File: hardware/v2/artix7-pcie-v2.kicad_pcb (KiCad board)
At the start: 4 copper layers, 60 x 51 mm, 187 parts, among them J1 Conn_02x20_Odd_Even, J10 USB_B_Micro, J2 Conn_02x20_Odd_Even, J4 USB3_A, J5 USB3_A_AS_PCIE, J6 JTAG, J7 Conn_01x02, J8 SER, SW1 PROG, SW2 USER, U1 XC7A75T-FGG484, U10 TPS74701DRCR, U2 MX25L51245GZ2I-10G, U3 TLV62569DBVR, U4 5P49V6965A000NLGI, U5 TLV62569PDDCR, U6 TLV62569DBVR, U7 TLV62569DBVR, U8 TLV62569DBVR, U9 TPS74701DRCR, X1 25MHz/10pF

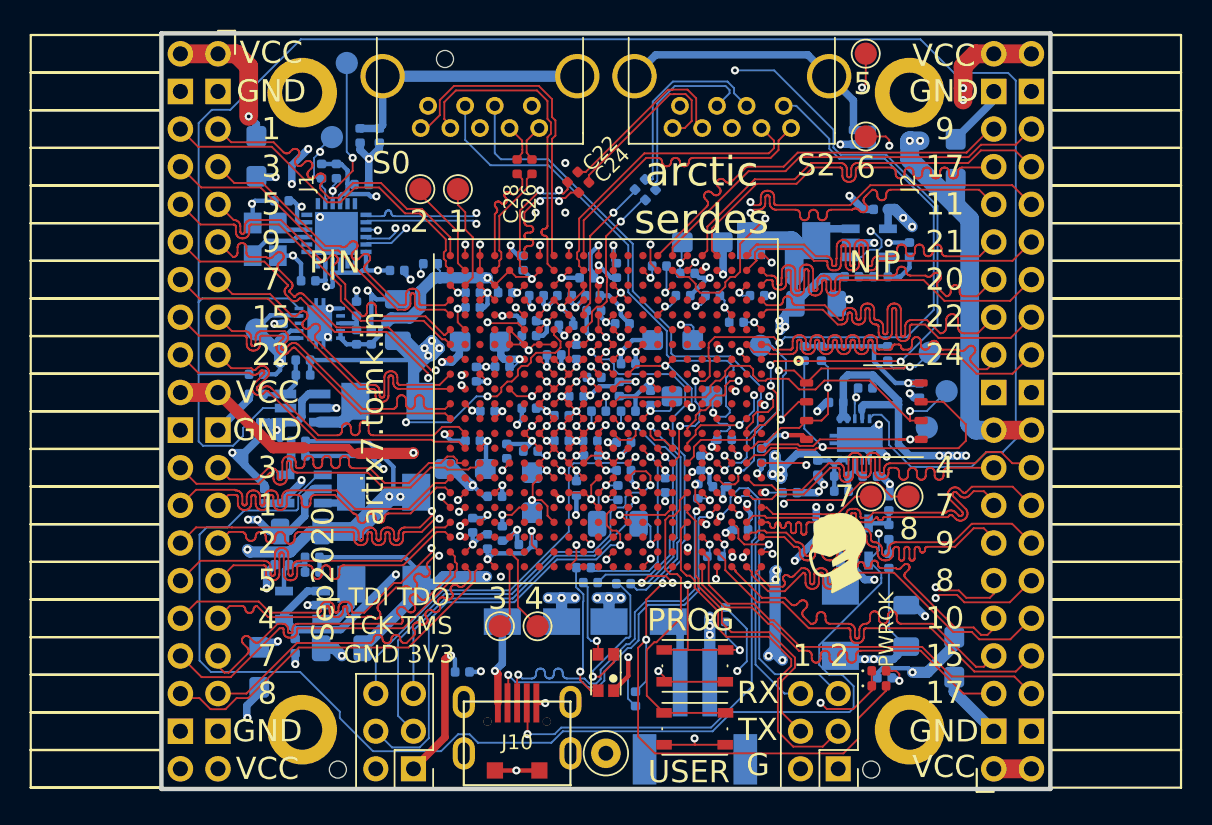
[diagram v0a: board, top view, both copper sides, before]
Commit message: v2 hardware: fixed drc issues from inductor pad changes
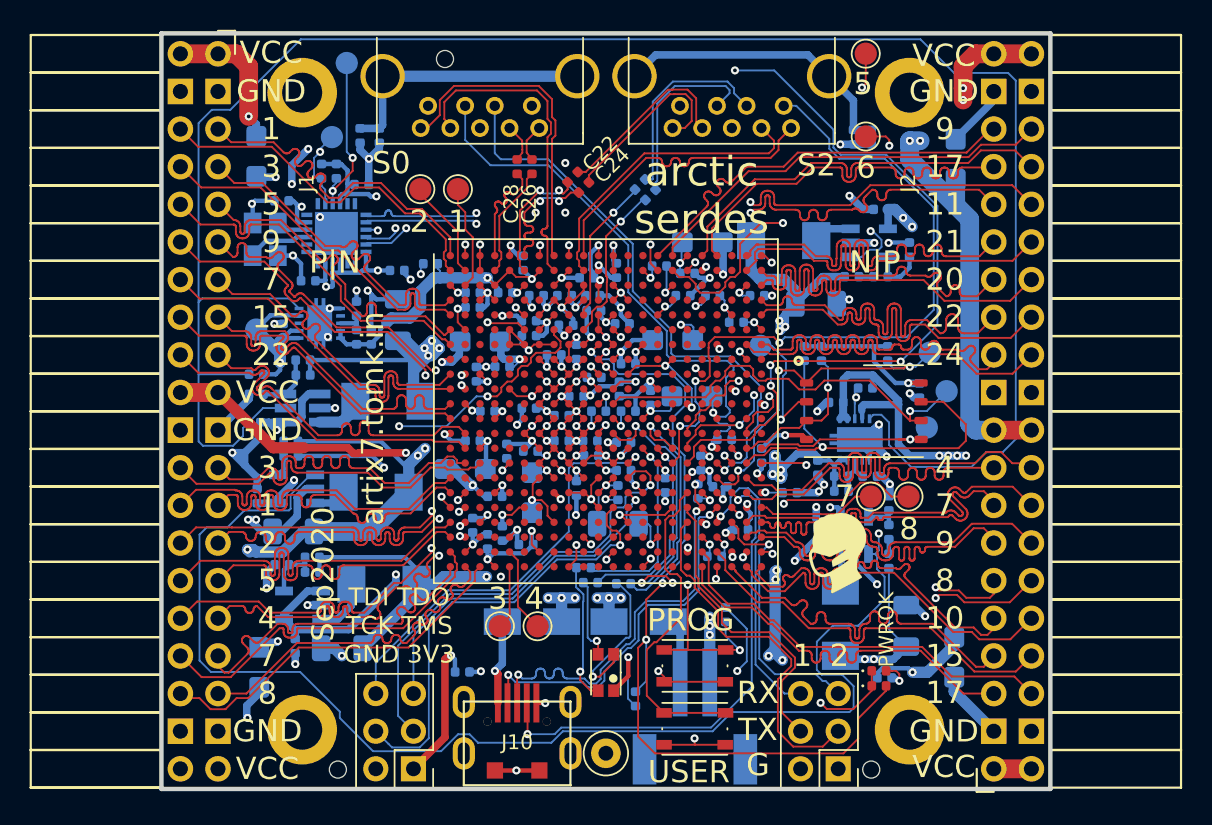
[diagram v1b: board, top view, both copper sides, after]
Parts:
- moved L3 0.51 mm to (125.6, 92.3)
- moved C12 0.51 mm to (120.0, 94.9)
- moved C8 0.51 mm to (117.6, 92.5)
- moved R18 0.51 mm to (119.8, 89.8)
- moved R19 0.51 mm to (119.8, 88.8)
- moved U6 0.51 mm to (120.2, 92.1)
- moved U3 0.45 mm to (157.9, 95.2)
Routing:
- net VCC: track 171.4 -> 169.6 mm
- net /Power/PG_1.8V: track 119.7 -> 121.1 mm
- net GND: track 277.9 -> 278.8 mm
- net /VCCO_16: track 103.0 -> 102.4 mm

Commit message: v2 hardware: change 100uF to 3528 for jlcpcb
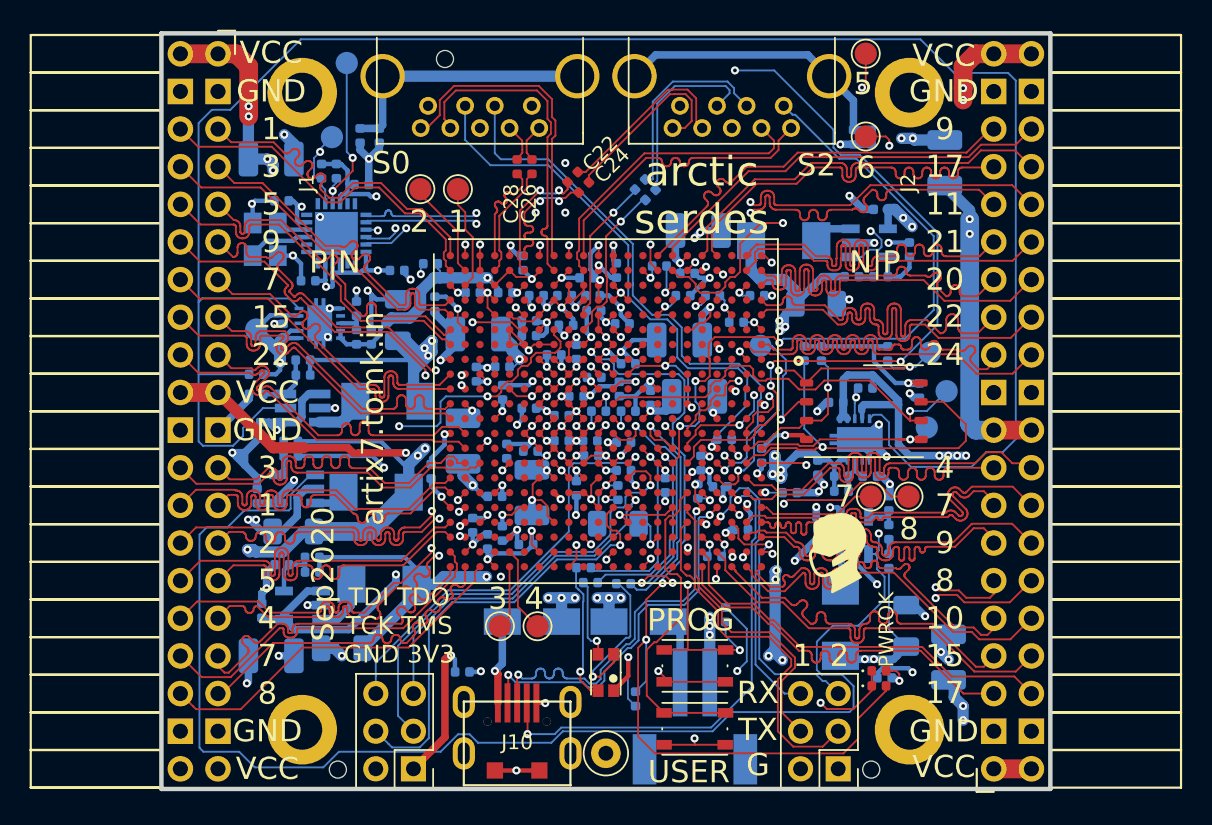
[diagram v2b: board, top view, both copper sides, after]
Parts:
- C18, C23, C42, C44, C60, C67, C68, C78, C85, C86: footprint tom-passives:CP_EIA-3216-12_Kemet-S -> tom-passives:CP_EIA-3528-15_AVX-H
- R26, R27, R34, R35: value 270R/5% -> 300R/5%
- R30: value 1k/1% -> 1.2k/1%
- moved C94 3.48 mm to (129.3, 90.9), turned to 270 degrees
- moved C11 3.29 mm to (117.9, 100.3), turned to 270 degrees
- moved C90 2.56 mm to (129.5, 79.6), turned to 270 degrees
- moved C85 1.89 mm to (131.5, 88.8), turned to 90 degrees
- moved C88 1.63 mm to (134.1, 85.5), turned to 90 degrees
- moved C18 1.12 mm to (118.5, 103.3), turned to 0 degrees
- moved C23 1.01 mm to (118.5, 69.8), turned to 0 degrees
- moved C78 0.84 mm to (147.3, 74.6)
- moved C68 0.77 mm to (164.0, 70.0)
- moved C86 0.52 mm to (132.5, 81.6)
- moved C42 0.46 mm to (146.1, 82.0)
- moved C67 0.38 mm to (164.2, 103.4), turned to 90 degrees
- moved C60 0.17 mm to (147.1, 85.8)
- turned C45 to 180 degrees
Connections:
- U1 pad A13: Net-(U1-PadA13) -> (no net)
- U1 pad A14: Net-(U1-PadA14) -> (no net)
- U1 pad A20: Net-(U1-PadA20) -> (no net)
- U1 pad AA10: Net-(U1-PadAA10) -> (no net)
- U1 pad AA11: Net-(U1-PadAA11) -> (no net)
- U1 pad AA13: Net-(U1-PadAA13) -> (no net)
- U1 pad AA14: Net-(U1-PadAA14) -> (no net)
- U1 pad AA15: Net-(U1-PadAA15) -> (no net)
- U1 pad AA16: Net-(U1-PadAA16) -> (no net)
- U1 pad AA3: Net-(U1-PadAA3) -> (no net)
- U1 pad AA4: Net-(U1-PadAA4) -> (no net)
- U1 pad AA6: Net-(U1-PadAA6) -> (no net)
- U1 pad AA8: Net-(U1-PadAA8) -> (no net)
- U1 pad AA9: Net-(U1-PadAA9) -> (no net)
- U1 pad AB10: Net-(U1-PadAB10) -> (no net)
- U1 pad AB11: Net-(U1-PadAB11) -> (no net)
- U1 pad AB12: Net-(U1-PadAB12) -> (no net)
- U1 pad AB13: Net-(U1-PadAB13) -> (no net)
- U1 pad AB15: Net-(U1-PadAB15) -> (no net)
- U1 pad AB16: Net-(U1-PadAB16) -> (no net)
- U1 pad AB17: Net-(U1-PadAB17) -> (no net)
- U1 pad AB6: Net-(U1-PadAB6) -> (no net)
- U1 pad AB7: Net-(U1-PadAB7) -> (no net)
- U1 pad AB8: Net-(U1-PadAB8) -> (no net)
- U1 pad B13: Net-(U1-PadB13) -> (no net)
- U1 pad B20: Net-(U1-PadB20) -> (no net)
- U1 pad C13: Net-(U1-PadC13) -> (no net)
- U1 pad C14: Net-(U1-PadC14) -> (no net)
- U1 pad C15: Net-(U1-PadC15) -> (no net)
- U1 pad C17: Net-(U1-PadC17) -> (no net)
- U1 pad C18: Net-(U1-PadC18) -> (no net)
- U1 pad C19: Net-(U1-PadC19) -> (no net)
- U1 pad C20: Net-(U1-PadC20) -> (no net)
- U1 pad C5: Net-(U1-PadC5) -> (no net)
- U1 pad C7: Net-(U1-PadC7) -> (no net)
- U1 pad D14: Net-(U1-PadD14) -> (no net)
- U1 pad D15: Net-(U1-PadD15) -> (no net)
- U1 pad D16: Net-(U1-PadD16) -> (no net)
- U1 pad D17: Net-(U1-PadD17) -> (no net)
- U1 pad D19: Net-(U1-PadD19) -> (no net)
- U1 pad D2: Net-(U1-PadD2) -> (no net)
- U1 pad D20: Net-(U1-PadD20) -> (no net)
- U1 pad D21: Net-(U1-PadD21) -> (no net)
- U1 pad D5: Net-(U1-PadD5) -> (no net)
- U1 pad D7: Net-(U1-PadD7) -> (no net)
- U1 pad E13: Net-(U1-PadE13) -> (no net)
- U1 pad E14: Net-(U1-PadE14) -> (no net)
- U1 pad E16: Net-(U1-PadE16) -> (no net)
- U1 pad E17: Net-(U1-PadE17) -> (no net)
- U1 pad E18: Net-(U1-PadE18) -> (no net)
- U1 pad E19: Net-(U1-PadE19) -> (no net)
- U1 pad E2: Net-(U1-PadE2) -> (no net)
- U1 pad E21: Net-(U1-PadE21) -> (no net)
- U1 pad E3: Net-(U1-PadE3) -> (no net)
- U1 pad F13: Net-(U1-PadF13) -> (no net)
- U1 pad F14: Net-(U1-PadF14) -> (no net)
- U1 pad F15: Net-(U1-PadF15) -> (no net)
- U1 pad F16: Net-(U1-PadF16) -> (no net)
- U1 pad F18: Net-(U1-PadF18) -> (no net)
- U1 pad F19: Net-(U1-PadF19) -> (no net)
- U1 pad F20: Net-(U1-PadF20) -> (no net)
- U1 pad F21: Net-(U1-PadF21) -> (no net)
- U1 pad F3: Net-(U1-PadF3) -> (no net)
- U1 pad F4: Net-(U1-PadF4) -> (no net)
- U1 pad G13: Net-(U1-PadG13) -> (no net)
- U1 pad G15: Net-(U1-PadG15) -> (no net)
- U1 pad G16: Net-(U1-PadG16) -> (no net)
- U1 pad G17: Net-(U1-PadG17) -> (no net)
- U1 pad G18: Net-(U1-PadG18) -> (no net)
- U1 pad G2: Net-(U1-PadG2) -> (no net)
- U1 pad G20: Net-(U1-PadG20) -> (no net)
- U1 pad G3: Net-(U1-PadG3) -> (no net)
- U1 pad G4: Net-(U1-PadG4) -> (no net)
- U1 pad H13: Net-(U1-PadH13) -> (no net)
- U1 pad H14: Net-(U1-PadH14) -> (no net)
- U1 pad H15: Net-(U1-PadH15) -> (no net)
- U1 pad H17: Net-(U1-PadH17) -> (no net)
- U1 pad H18: Net-(U1-PadH18) -> (no net)
- U1 pad H19: Net-(U1-PadH19) -> (no net)
- U1 pad H2: Net-(U1-PadH2) -> (no net)
- U1 pad H20: Net-(U1-PadH20) -> (no net)
- U1 pad H22: Net-(U1-PadH22) -> (no net)
- U1 pad H3: Net-(U1-PadH3) -> (no net)
- U1 pad H4: Net-(U1-PadH4) -> (no net)
- U1 pad H5: Net-(U1-PadH5) -> (no net)
- U1 pad J14: Net-(U1-PadJ14) -> (no net)
- U1 pad J15: Net-(U1-PadJ15) -> (no net)
- U1 pad J16: Net-(U1-PadJ16) -> (no net)
- U1 pad J17: Net-(U1-PadJ17) -> (no net)
- U1 pad J19: Net-(U1-PadJ19) -> (no net)
- U1 pad J20: Net-(U1-PadJ20) -> (no net)
- U1 pad J21: Net-(U1-PadJ21) -> (no net)
- U1 pad J22: Net-(U1-PadJ22) -> (no net)
- U1 pad J4: Net-(U1-PadJ4) -> (no net)
- U1 pad J5: Net-(U1-PadJ5) -> (no net)
- U1 pad J6: Net-(U1-PadJ6) -> (no net)
- U1 pad K13: Net-(U1-PadK13) -> (no net)
- U1 pad K14: Net-(U1-PadK14) -> (no net)
- U1 pad K16: Net-(U1-PadK16) -> (no net)
- U1 pad K17: Net-(U1-PadK17) -> (no net)
- U1 pad K18: Net-(U1-PadK18) -> (no net)
- U1 pad K19: Net-(U1-PadK19) -> (no net)
- U1 pad K21: Net-(U1-PadK21) -> (no net)
- U1 pad K22: Net-(U1-PadK22) -> (no net)
- U1 pad K3: Net-(U1-PadK3) -> (no net)
- U1 pad K4: Net-(U1-PadK4) -> (no net)
- U1 pad K6: Net-(U1-PadK6) -> (no net)
- U1 pad L13: Net-(U1-PadL13) -> (no net)
- U1 pad L14: Net-(U1-PadL14) -> (no net)
- U1 pad L15: Net-(U1-PadL15) -> (no net)
- U1 pad L16: Net-(U1-PadL16) -> (no net)
- U1 pad L18: Net-(U1-PadL18) -> (no net)
- U1 pad L19: Net-(U1-PadL19) -> (no net)
- U1 pad L20: Net-(U1-PadL20) -> (no net)
- U1 pad L21: Net-(U1-PadL21) -> (no net)
- U1 pad L3: Net-(U1-PadL3) -> (no net)
- U1 pad L4: Net-(U1-PadL4) -> (no net)
- U1 pad L5: Net-(U1-PadL5) -> (no net)
- U1 pad L6: Net-(U1-PadL6) -> (no net)
- U1 pad M13: Net-(U1-PadM13) -> (no net)
- U1 pad M15: Net-(U1-PadM15) -> (no net)
- U1 pad M16: Net-(U1-PadM16) -> (no net)
- U1 pad M17: Net-(U1-PadM17) -> (no net)
- U1 pad M18: Net-(U1-PadM18) -> (no net)
- U1 pad M2: Net-(U1-PadM2) -> (no net)
- U1 pad M20: Net-(U1-PadM20) -> (no net)
- U1 pad M21: Net-(U1-PadM21) -> (no net)
- U1 pad M22: Net-(U1-PadM22) -> (no net)
- U1 pad M3: Net-(U1-PadM3) -> (no net)
- U1 pad M5: Net-(U1-PadM5) -> (no net)
- U1 pad M6: Net-(U1-PadM6) -> (no net)
- U1 pad N13: Net-(U1-PadN13) -> (no net)
- U1 pad N14: Net-(U1-PadN14) -> (no net)
- U1 pad N15: Net-(U1-PadN15) -> (no net)
- U1 pad N18: Net-(U1-PadN18) -> (no net)
- U1 pad N19: Net-(U1-PadN19) -> (no net)
- U1 pad N20: Net-(U1-PadN20) -> (no net)
- U1 pad N22: Net-(U1-PadN22) -> (no net)
- U1 pad N3: Net-(U1-PadN3) -> (no net)
- U1 pad N4: Net-(U1-PadN4) -> (no net)
- U1 pad N5: Net-(U1-PadN5) -> (no net)
- U1 pad P1: Net-(U1-PadP1) -> (no net)
- U1 pad P4: Net-(U1-PadP4) -> (no net)
- U1 pad P5: Net-(U1-PadP5) -> (no net)
- U1 pad P6: Net-(U1-PadP6) -> (no net)
- U1 pad R1: Net-(U1-PadR1) -> (no net)
- U1 pad R14: Net-(U1-PadR14) -> (no net)
- U1 pad R18: Net-(U1-PadR18) -> (no net)
- U1 pad R4: Net-(U1-PadR4) -> (no net)
- U1 pad R6: Net-(U1-PadR6) -> (no net)
- U1 pad T14: Net-(U1-PadT14) -> (no net)
- U1 pad T15: Net-(U1-PadT15) -> (no net)
- U1 pad T16: Net-(U1-PadT16) -> (no net)
- U1 pad T18: Net-(U1-PadT18) -> (no net)
- U1 pad T20: Net-(U1-PadT20) -> (no net)
- U1 pad T3: Net-(U1-PadT3) -> (no net)
- U1 pad T4: Net-(U1-PadT4) -> (no net)
- U1 pad T5: Net-(U1-PadT5) -> (no net)
- U1 pad T6: Net-(U1-PadT6) -> (no net)
- U1 pad U15: Net-(U1-PadU15) -> (no net)
- U1 pad U16: Net-(U1-PadU16) -> (no net)
- U1 pad U3: Net-(U1-PadU3) -> (no net)
- U1 pad U5: Net-(U1-PadU5) -> (no net)
- U1 pad U6: Net-(U1-PadU6) -> (no net)
- U1 pad U7: Net-(U1-PadU7) -> (no net)
- U1 pad V10: Net-(U1-PadV10) -> (no net)
- U1 pad V13: Net-(U1-PadV13) -> (no net)
- U1 pad V14: Net-(U1-PadV14) -> (no net)
- U1 pad V15: Net-(U1-PadV15) -> (no net)
- U1 pad V3: Net-(U1-PadV3) -> (no net)
- U1 pad V4: Net-(U1-PadV4) -> (no net)
- U1 pad V5: Net-(U1-PadV5) -> (no net)
- U1 pad V7: Net-(U1-PadV7) -> (no net)
- U1 pad V8: Net-(U1-PadV8) -> (no net)
- U1 pad V9: Net-(U1-PadV9) -> (no net)
- U1 pad W10: Net-(U1-PadW10) -> (no net)
- U1 pad W11: Net-(U1-PadW11) -> (no net)
- U1 pad W12: Net-(U1-PadW12) -> (no net)
- U1 pad W14: Net-(U1-PadW14) -> (no net)
- U1 pad W15: Net-(U1-PadW15) -> (no net)
- U1 pad W16: Net-(U1-PadW16) -> (no net)
- U1 pad W4: Net-(U1-PadW4) -> (no net)
- U1 pad W5: Net-(U1-PadW5) -> (no net)
- U1 pad W6: Net-(U1-PadW6) -> (no net)
- U1 pad W7: Net-(U1-PadW7) -> (no net)
- U1 pad W9: Net-(U1-PadW9) -> (no net)
- U1 pad Y11: Net-(U1-PadY11) -> (no net)
- U1 pad Y12: Net-(U1-PadY12) -> (no net)
- U1 pad Y13: Net-(U1-PadY13) -> (no net)
- U1 pad Y14: Net-(U1-PadY14) -> (no net)
- U1 pad Y16: Net-(U1-PadY16) -> (no net)
- U1 pad Y17: Net-(U1-PadY17) -> (no net)
- U1 pad Y3: Net-(U1-PadY3) -> (no net)
- U1 pad Y4: Net-(U1-PadY4) -> (no net)
- U1 pad Y6: Net-(U1-PadY6) -> (no net)
- U1 pad Y7: Net-(U1-PadY7) -> (no net)
- U1 pad Y8: Net-(U1-PadY8) -> (no net)
- U1 pad Y9: Net-(U1-PadY9) -> (no net)
- U10 pad 7: Net-(U10-Pad7) -> (no net)
- U4 pad 1: Net-(U4-Pad1) -> (no net)
- U4 pad 11: Net-(U4-Pad11) -> (no net)
- U4 pad 12: Net-(U4-Pad12) -> (no net)
- U4 pad 19: Net-(U4-Pad19) -> (no net)
- U4 pad 2: Net-(U4-Pad2) -> (no net)
- U4 pad 20: Net-(U4-Pad20) -> (no net)
- U4 pad 24: Net-(U4-Pad24) -> (no net)
- U4 pad 6: Net-(U4-Pad6) -> (no net)
- U4 pad 7: Net-(U4-Pad7) -> (no net)
- U9 pad 3: Net-(U9-Pad3) -> (no net)
- U9 pad 7: Net-(U9-Pad7) -> (no net)
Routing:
- net /VBUS: track 70.6 -> 80.0 mm, vias 3 -> 1
- net GND: track 278.8 -> 283.7 mm, vias 123 -> 127
- net /Power/PG_1.8V: track 121.1 -> 125.2 mm
- net /VCCO_16: track 102.4 -> 99.8 mm
- net /PCIE_WAKE: track 47.3 -> 45.7 mm
- net +3V3: track 261.0 -> 259.8 mm, vias 25 -> 27
- net /PCIE_PERST: track 54.7 -> 53.7 mm
- net VCC: track 169.6 -> 170.5 mm
- net /artix7-pcie-v2-serdes/MGTRREF: track 27.5 -> 28.3 mm
- net /VCCO_34: track 171.0 -> 170.3 mm, vias 18 -> 21
- net /S0_USB2_N: track 38.2 -> 38.8 mm
- net +1V8: track 43.7 -> 44.2 mm
- net +1V0: track 61.4 -> 61.7 mm, vias 21 -> 20

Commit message: v2 hardware: fix drc/unrouted ready for resubmission to JLC
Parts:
- moved C73 0.91 mm to (135.4, 88.9), turned to 90 degrees
- moved C95 0.73 mm to (134.1, 95.8)
- moved C91 0.66 mm to (134.4, 88.8)
- moved C87 0.19 mm to (133.4, 92.6)
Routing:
- net GND: track 283.7 -> 290.3 mm, vias 127 -> 128

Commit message: hardware: update pcb as per sep 2020b
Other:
- rule pad_to_mask_clearance: 0.01 -> 0

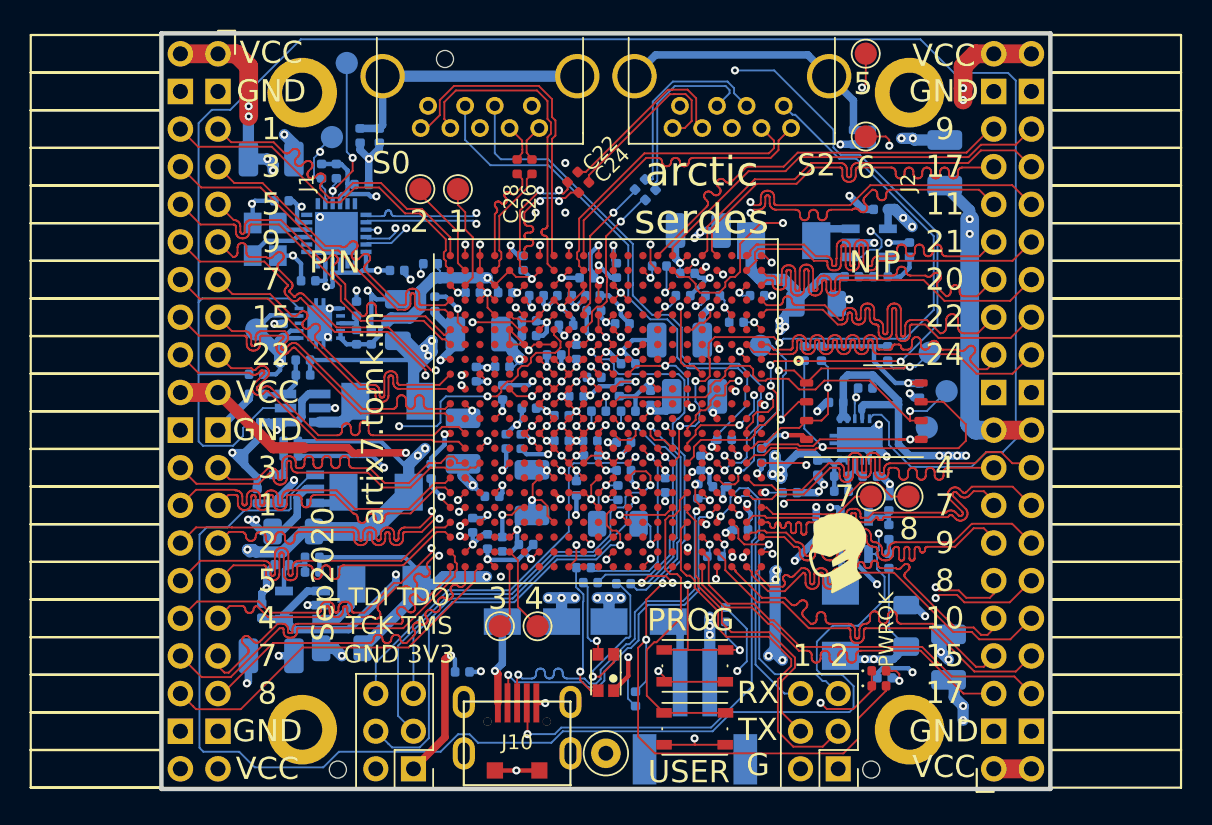
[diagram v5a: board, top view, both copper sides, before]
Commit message: Re-route HS diff pairs for 90R (0.147/0.253 as per RPI cm4 carrier) Add ground stitching
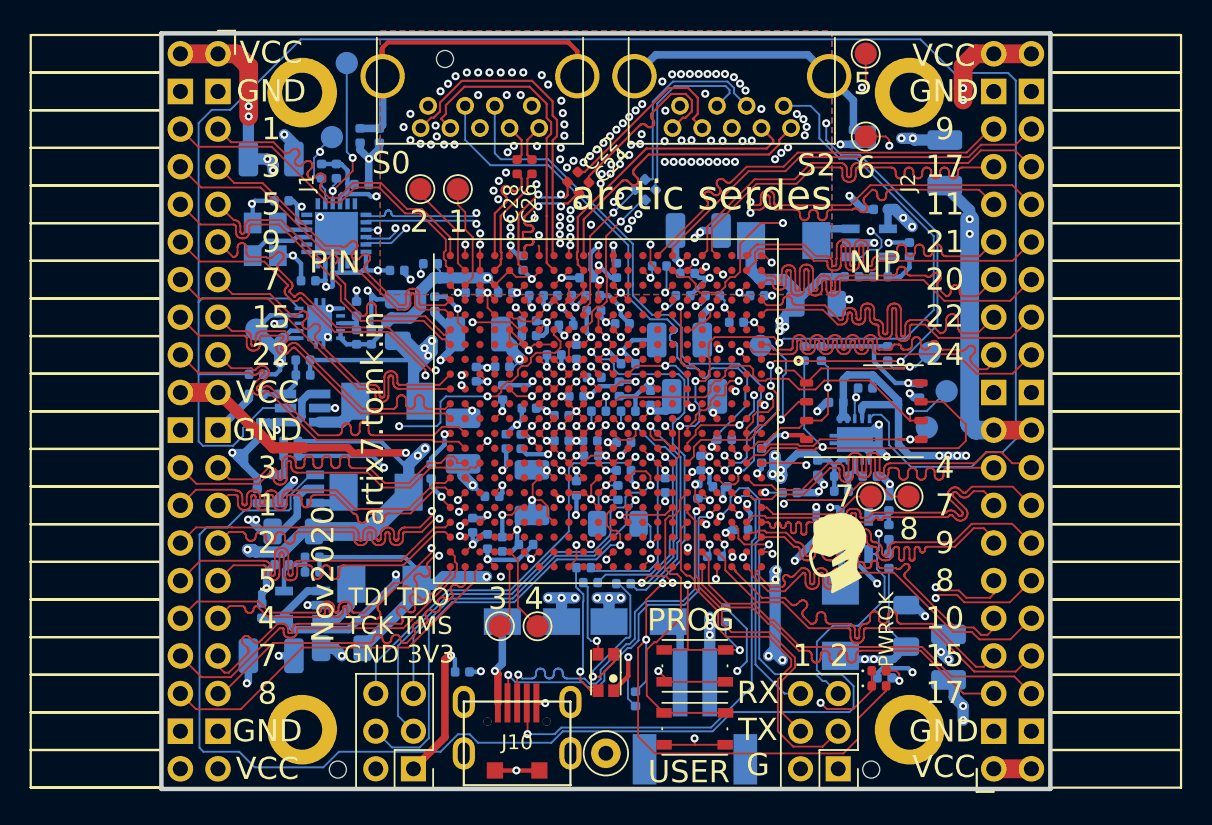
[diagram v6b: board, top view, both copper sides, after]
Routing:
- net /artix7-pcie-v2-bank14/IO_L8_14_N: track 21.4 -> 27.0 mm
- net Net-(C3-Pad1): track 18.1 -> 22.1 mm
- net /CLK_SCL: track 55.6 -> 53.1 mm
- net /CLK_SDA: track 54.9 -> 53.6 mm
- net /S0_USB2_P: track 37.6 -> 38.9 mm
- net GND: track 290.3 -> 289.3 mm, vias 128 -> 241
- net /PCIE_WAKE: track 45.7 -> 46.7 mm
- net /PCIE_PERST: track 53.7 -> 53.1 mm
- net VCC: track 170.5 -> 170.0 mm
- added copper zone on B.Cu, net GND
- added copper zone on F.Cu, net GND
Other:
- board text added: "Nov2020"
- board text removed: "Sep2020"
